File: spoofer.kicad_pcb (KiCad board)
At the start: 2 copper layers, 6 parts, among them J1 HDMI_A, J2 Conn_01x02, J3 HDMI_A, J4 Conn_01x03, J5 Conn_01x03, U1 AT24CS02-SSHM

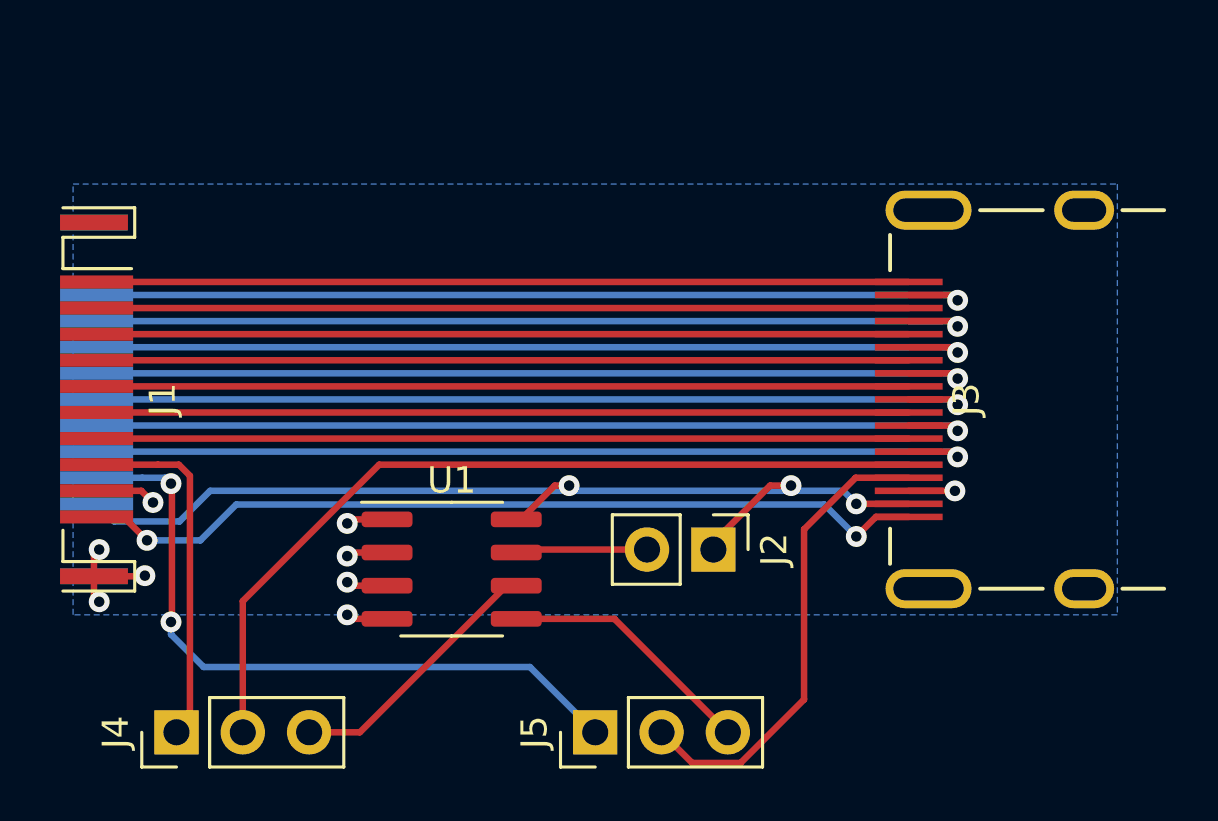
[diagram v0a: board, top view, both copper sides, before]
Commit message: Redesign board
Now it is smaller.
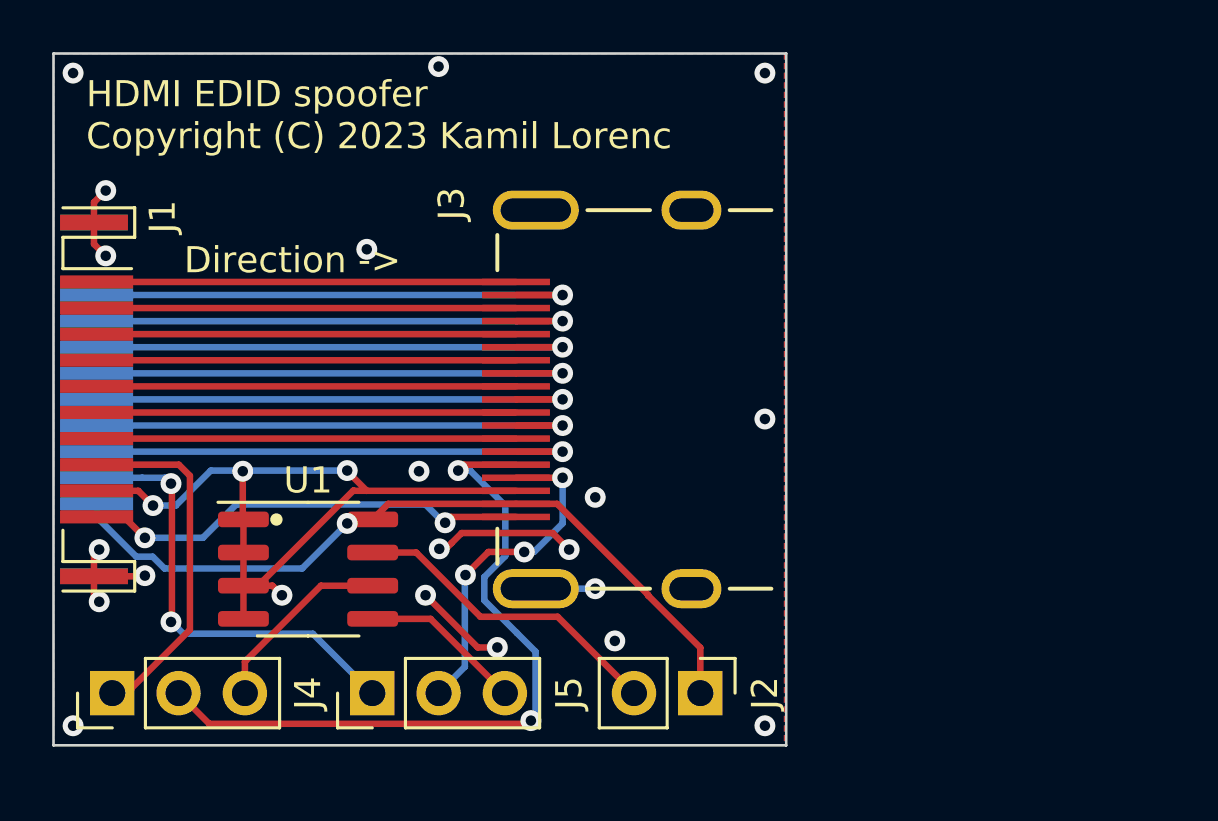
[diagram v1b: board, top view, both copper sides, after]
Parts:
- moved J3 15.0 mm to (177.8, 106.0)
- moved J5 8.67 mm to (169.0, 117.2)
- moved J2 5.52 mm to (181.5, 117.2)
- moved U1 5.50 mm to (166.5, 112.5)
- moved J4 2.88 mm to (159.0, 117.2)
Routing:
- net GND: track 14.6 -> 48.6 mm, vias 9 -> 24
- net /D1_n: track 35.5 -> 19.6 mm
- net /HPD: track 32.9 -> 17.3 mm
- net /D2S: track 35.0 -> 19.6 mm
- net /CK_n: track 35.0 -> 19.6 mm
- net /D0S: track 35.0 -> 19.6 mm
- net /D1_p: track 35.0 -> 19.6 mm
- net /CK_p: track 35.0 -> 19.6 mm
- net /UTIL: track 35.0 -> 19.6 mm
- net /Do_p: track 31.1 -> 16.1 mm
- net /D2_p: track 31.1 -> 16.1 mm
- net /D2_n: track 31.1 -> 16.1 mm
- net /D1S: track 31.1 -> 16.1 mm
- net /D0_n: track 31.1 -> 16.1 mm
- net /CKS: track 31.1 -> 16.1 mm
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- added copper zone on F.Cu, net GND
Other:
- board outline added: 28.1 x 26.5 mm
- board text added: "<- Direction"
- board text added: "Direction ->"
- board text added: "HDMI EDID spoofer Copyright (C) 2023 Kamil Lorenc"

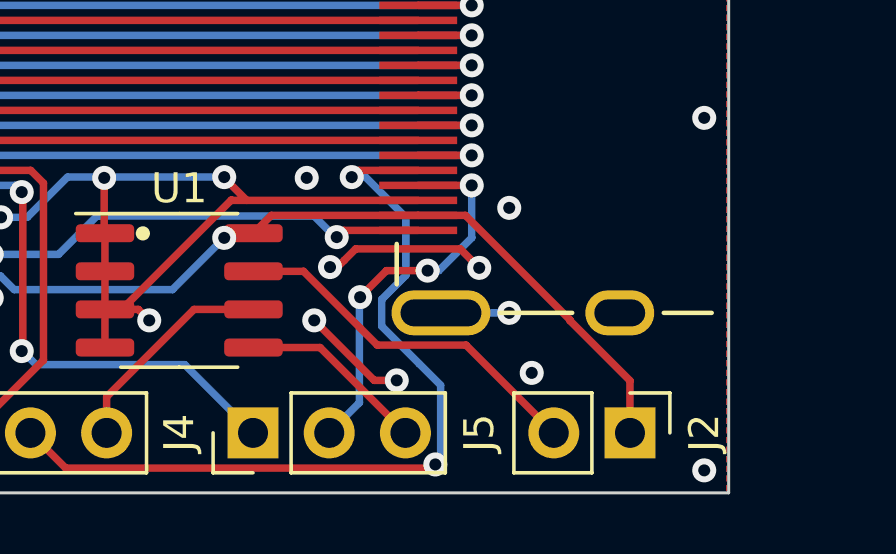
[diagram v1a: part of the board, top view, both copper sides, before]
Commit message: Add silkscreen help
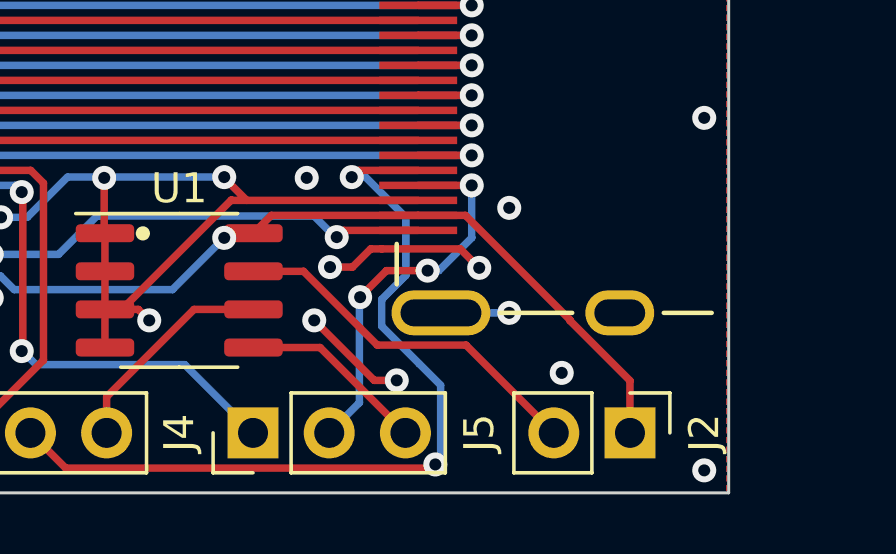
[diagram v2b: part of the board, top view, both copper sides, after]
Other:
- board text added: "Fit to WP"
- board text added: "| Pass Force |"
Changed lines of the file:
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@@
     (effects (font (size 1 1) (thickness 0.15)) (justify left bottom mirror))
+  )
+  (gr_text "    |   Pass\nForce  |" (at 165.5 115.75) (layer "B.SilkS")
+    (effects (font (size 0.8 0.8) (thickness 0.12)) (justify left bottom mirror))
+  )
+  (gr_text "    |   Pass\nForce  |" (at 175.25 115.75) (layer "B.SilkS")
+    (effects (font (size 0.8 0.8) (thickness 0.12)) (justify left bottom mirror))
+  )
+  (gr_text "Fit to WP" (at 183 115.75) (layer "B.SilkS")
+    (effects (font (size 0.8 0.8) (thickness 0.12)) (justify left bottom mirror))
   )
   (gr_text "HDMI EDID spoofer\nCopyright (C) 2023 Kamil Lorenc" (at 158 96.5) (layer "F.SilkS")
@@
   (segment (start 164.025 113.135) (end 164.025 114.405) (width 0.25) (layer "F.Cu") (net 7))
   (segment (start 158.3 99.225) (end 158.3 98.45) (width 0.25) (layer "F.Cu") (net 7))
+  (segment (start 172.882997 111.117003) (end 172.276596 111.723404) (width 0.25) (layer "F.Cu") (net 7))
   (segment (start 158.3 99.225) (end 158.3 100.05) (width 0.25) (layer "F.Cu") (net 7))
   (segment (start 164 108.75) (end 164 110.57) (width 0.25) (layer "F.Cu") (net 7))
-  (segment (start 172.382802 111.117003) (end 171.999805 111.5) (width 0.25) (layer "F.Cu") (net 7))
   (segment (start 164.025 113.135) (end 165.135 113.135) (width 0.25) (layer "F.Cu") (net 7))
   (segment (start 168.75 109.5) (end 168.25 109.5) (width 0.25) (layer "F.Cu") (net 7))
+  (segment (start 173.25 111.117003) (end 172.882997 111.117003) (width 0.25) (layer "F.Cu") (net 7))
   (segment (start 164.025 111.865) (end 164.025 113.135) (width 0.25) (layer "F.Cu") (net 7))
   (segment (start 158.3 98.45) (end 158.75 98) (width 0.25) (layer "F.Cu") (net 7))
   (segment (start 164 110.57) (end 164.025 110.595) (width 0.25) (layer "F.Cu") (net 7))
+  (segment (start 173.25 111.117003) (end 175.867003 111.117003) (width 0.25) (layer "F.Cu") (net 7))
   (segment (start 158.3 112.775) (end 160.225 112.775) (width 0.25) (layer "F.Cu") (net 7))
   (segment (start 158.3 113.55) (end 158.5 113.75) (width 0.25) (layer "F.Cu") (net 7))
   (segment (start 168 108.7245) (end 168 108.75) (width 0.25) (layer "F.Cu") (net 7))
-  (segment (start 175.867003 111.117003) (end 172.382802 111.117003) (width 0.25) (layer "F.Cu") (net 7))
   (segment (start 158.3 111.95) (end 158.5 111.75) (width 0.25) (layer "F.Cu") (net 7))
-  (segment (start 171.999805 111.5) (end 171.776401 111.723404) (width 0.25) (layer "F.Cu") (net 7))
   (segment (start 164.515 113.209694) (end 168.237347 109.487347) (width 0.25) (layer "F.Cu") (net 7))
   (segment (start 171 113.5) (end 173 115.5) (width 0.25) (layer "F.Cu") (net 7))
+  (segment (start 175.867003 111.117003) (end 176.5 111.75) (width 0.25) (layer "F.Cu") (net 7))
   (segment (start 159.996994 109.5) (end 158.4 109.5) (width 0.25) (layer "F.Cu") (net 7))
   (segment (start 165.135 113.135) (end 165.5 113.5) (width 0.25) (layer "F.Cu") (net 7))
@@
   (segment (start 168 108.75) (end 168.75 109.5) (width 0.25) (layer "F.Cu") (net 7))
   (segment (start 158.3 112.775) (end 158.3 111.95) (width 0.25) (layer "F.Cu") (net 7))
+  (segment (start 172.276596 111.723404) (end 171.526596 111.723404) (width 0.25) (layer "F.Cu") (net 7))
   (segment (start 173 115.5) (end 173.75 115.5) (width 0.25) (layer "F.Cu") (net 7))
-  (segment (start 171.776401 111.723404) (end 171.526596 111.723404) (width 0.25) (layer "F.Cu") (net 7))
-  (segment (start 176.5 111.75) (end 175.867003 111.117003) (width 0.25) (layer "F.Cu") (net 7))
   (via (at 158.5 113.75) (size 0.8) (drill 0.4) (layers "F.Cu" "B.Cu") (net 7))
   (via (at 158.75 100.5) (size 0.8) (drill 0.4) (layers "F.Cu" "B.Cu") (net 7))
@@
   (via (at 160.561532 110.064538) (size 0.8) (drill 0.4) (layers "F.Cu" "B.Cu") (net 7))
   (via (at 164 108.75) (size 0.8) (drill 0.4) (layers "F.Cu" "B.Cu") (net 7))
-  (via (at 178.25 115.25) (size 0.8) (drill 0.4) (layers "F.Cu" "B.Cu") (free) (net 7))
+  (via (at 179.25 115.25) (size 0.8) (drill 0.4) (layers "F.Cu" "B.Cu") (free) (net 7))
   (via (at 168 108.7245) (size 0.8) (drill 0.4) (layers "F.Cu" "B.Cu") (net 7))
   (via (at 176.5 111.75) (size 0.8) (drill 0.4) (layers "F.Cu" "B.Cu") (free) (net 7))
